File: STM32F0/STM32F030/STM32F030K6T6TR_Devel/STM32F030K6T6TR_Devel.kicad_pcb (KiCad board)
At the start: 4 copper layers, 69 x 50 mm, 36 parts, among them J1 Conn_01x06, J2 Conn_02x03_Odd_Even, J3 Conn_02x10_Odd_Even, J4 Conn_01x16, J5 Conn_01x16, J6 Conn_02x05 Odd_Even, J7 Conn_02x03_Odd_Even, SW1 SW_Push, SW2 SW_DIP_x02, U1 STM32F030K6Tx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

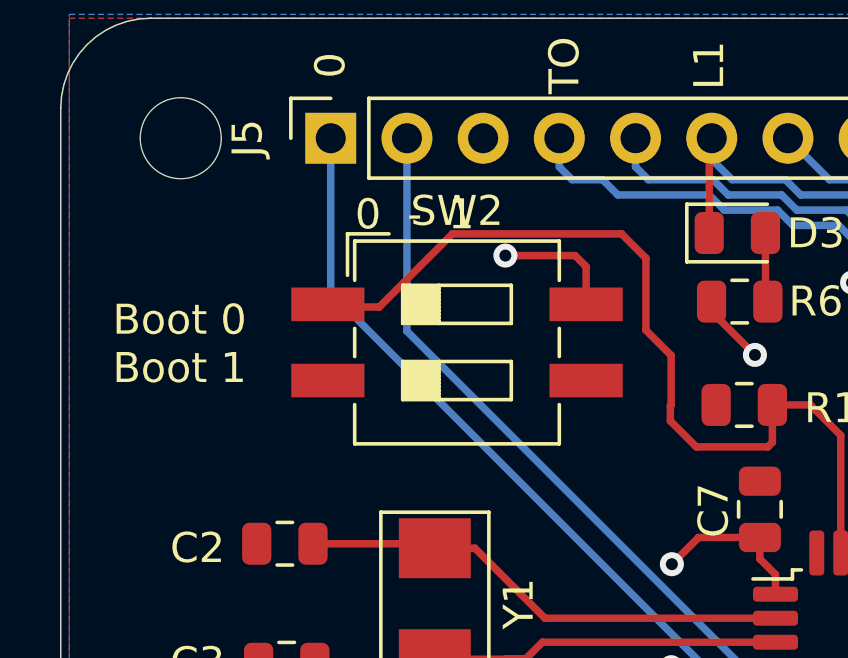
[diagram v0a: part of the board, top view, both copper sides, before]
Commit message: Kibot Split on files
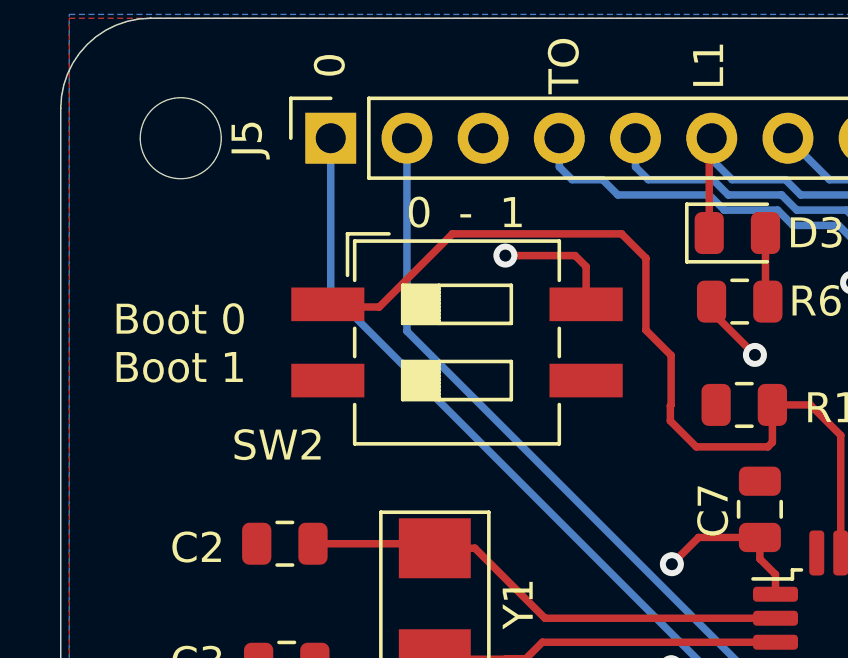
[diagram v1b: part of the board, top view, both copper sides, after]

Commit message: F030K6 Board
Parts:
- J3: value Conn_02x10_Odd_Even -> Conn_01x06; footprint Connector_PinHeader_2.54mm:PinHeader_2x10_P2.54mm_Vertical -> Connector_PinHeader_2.54mm:PinHeader_1x06_P2.54mm_Vertical
- J6: footprint Connector_PinHeader_1.27mm:PinHeader_2x05_P1.27mm_Vertical -> Connector_PinHeader_1.27mm:PinHeader_2x05_P1.27mm_Vertical_SMD
- moved J3 9.12 mm to (163.8, 95.4)
- moved J6 6.40 mm to (162.1, 87.0), turned to 180 degrees
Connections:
- J1 pad 1: /f_DTR -> (no net)
- J1 pad 5: /f_CTS -> (no net)
- J3 pad 2: VCC -> /PA14
- J3 pad 3: Net-(J3-Pad3) -> GND
- J3 pad 4: GND -> /PA13
- J3 pad 5: Net-(J3-Pad5) -> /STM32F030K6/NRST
- J3 pad 6: GND -> /PB3
- J5 pad 3: Net-(J5-Pad3) -> (no net)
- J6 pad 7: Net-(J6-Pad7) -> (no net)
- J6 pad 8: Net-(J6-Pad8) -> (no net)
- SW2 pad 2: Net-(SW2-Pad2) -> (no net)
- SW2 pad 3: Net-(SW2-Pad3) -> (no net)
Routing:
- net /STM32F030K6/NRST: track 96.8 -> 106.4 mm
- net /PB3: track 79.6 -> 85.7 mm
- net VCC: track 44.5 -> 50.4 mm
- net /PA14: track 83.7 -> 78.1 mm
- net GND: vias 4 -> 2
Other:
- board text added: "5V"
- board text added: "GND"
- board text added: "Rx"
- board text added: "Tx"

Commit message: Uart Changes
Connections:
- J1 pad 2: /PA9 -> /PA2
- J1 pad 3: /PA10 -> /PA3
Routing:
- net /PA3: track 27.2 -> 69.6 mm, vias 0 -> 1
- net /PA2: track 26.5 -> 66.7 mm, vias 0 -> 1
- net /PA10: track 64.2 -> 28.5 mm, vias 1 -> 0
- net /PA9: track 61.3 -> 28.8 mm, vias 1 -> 0
- net /PB0: track 38.5 -> 39.4 mm
- net GND: vias 2 -> 3
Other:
- board text added: "FTDI:"
- board text added: "SCL"
- board text added: "SDA"
- board text added: "STM32F030K6T Devel Board v2"

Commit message: Doc updated
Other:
- board text added: "CTS"
- board text added: "MISO"
- board text added: "MOSI"
- board text added: "NSS"
- board text added: "RTS"
- board text added: "SCK"

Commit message: STM32F030 Updated to kicad8
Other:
- net class 5V removed
- net class Default removed

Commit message: Add mpn for pcbway
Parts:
- J5: value Conn_01x16 -> Conn_01x08
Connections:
- net /STM32F030K6/NRST renamed /STM32F030K6/RST
- net /STM32F030K6/PF0 renamed /STM32F030K6/OSC_IN
- net /STM32F030K6/PF1 renamed /STM32F030K6/OSC_OUT
- J1 pad 1: (no net) -> /f_DTR
- J1 pad 5: (no net) -> /f_CTS
- J5 pad 3: (no net) -> unconnected-(J5-Pin_3-Pad3)
- J6 pad 7: (no net) -> unconnected-(J6-Pin_7-Pad7)
- J6 pad 8: (no net) -> unconnected-(J6-Pin_8-Pad8)
- SW2 pad 2: (no net) -> unconnected-(SW2-Pad2)
- SW2 pad 3: (no net) -> unconnected-(SW2-Pad3)
